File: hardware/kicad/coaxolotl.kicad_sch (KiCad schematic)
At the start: 0 parts

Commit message: Schematic v0.2: Olimex-style redraw with block diagram
- power/ground only as power symbols (project rails VCOAX, VMAIN, VHOLD, VLED, LNA_VCC)
- wires inside blocks, hierarchical labels + sheet pins between sheets (no global labels)
- Value carries critical parameters, blue design-intent notes, bold italic block titles
- sheet 1: block diagram + wired hierarchy; RF/Panel placeholders with reset-safe pulls
- pull-downs moved to the receiving parts (TPS2553 EN, RF switches), RC filters to the ADC pins
- check.py compares net partitions (catches shorts and splits), generator flags 4-way junctions
- net classes in .kicad_pro (POWER 0.4 mm <= 1.25 x SC-70 pad)

Co-Authored-By: Claude Opus 5.5 <noreply@anthropic.com>
Claude-Session: https://claude.ai/code/session_01YRUiF8Vp4242sya9Xyg3TV
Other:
- added sheet Panel (panel.kicad_sch)
- added sheet RF (rf.kicad_sch)
- sheet MCU ports: added FAULT_N, FMN, ILNA, LED_OE_N, LED_RCK, LED_SCK, LED_SER, LNA_EN, LNA_PATH, SCAP_ADC, SENSE, SW_V1, SW_V2, SW_V3; removed none
- sheet Power ports: added FAULT_N, ILNA, LNA_EN, SCAP_ADC, SENSE; removed none
- note added: "+3V3"
- note added: "20 kHz-2 GHz"
- note added: "330uF || 0.1F"
- note added: "3V3 LDO"
- note added: "6x 74HC595, 48 lamps"
- note added: "8 FILTERS"
- note added: "88-108 MHz, opt."
- note added: "<- DC 4.5 V + OOK"
- note added: "ANTENNA"
- note added: "BIAS-T"
- note added: "COAX"
- note added: "Coaxolotl - block diagram"
- note added: "F0 THRU..F7"
- note added: "FB + 47uF"
- note added: "FM NOTCH"
- note added: "FMN"
- note added: "FRONT PANEL"
- note added: "GDT, limiter"
- note added: "HOLD-UP"
- note added: "HPF 25M, LPF 2.2G"
- note added: "IDEAL DIODE"
- note added: "LAMP RAIL"
- note added: "LED bus"
- note added: "LM66100"
- note added: "LNA"
- note added: "LNA SUPPLY"
- note added: "LNA_PATH"
- note added: "LNA_VCC"
- note added: "MCP1700"
- note added: "MCU (sheet 3)"
- note added: "MCU EFM8BB21"
- note added: "PE42520"
- note added: "PE42582"
- note added: "PRESELECTOR"
- note added: "PROTECTION"
- note added: "Power and ground cross sheets only as power symbols (VCOAX, VMAIN, VHOLD, VLED, LNA_VCC, +3V3, GND)."
- note added: "RF -> RTL-SDR V3"
- note added: "RF signal path (sheet 4)"
- note added: "SENSE, 680R, PWR"
- note added: "SP8T"
- note added: "SPDT"
- note added: "SW_V1..3"
- note added: "Sheets"
- note added: "Signals cross sheets as hierarchical labels through the sheet pins above. Firmware pin map: firmware/src/hal_efm8bb2.c"
- note added: "TPS2553+INA180"
- note added: "VCOAX"
- note added: "VCOAX TAP"
- note added: "VHOLD"
- note added: "VLED"
- note added: "VMAIN"
- note added: "bypass (F1-F4 force it: AUTO)"
- note added: "control (blue, dashed): LNA_PATH, SW_V1..3, FMN, LNA_EN"
- note added: "decodes OOK on SENSE, Snooze when idle"
- note added: "monitors SENSE, SCAP_ADC, ILNA, FAULT_N"
- note added: "panel (sheet 5)"
- note added: "power (sheet 2)"
- note added: "~100 mA"
- note removed: "2 Power - VCOAX tap, LM66100 ideal diode, TPS2553 + INA180 LNA supply, hold-up, 3V3 [this review]"
- note removed: "3 MCU - EFM8BB21F16G, C2, reset-safe pulls, test points [this review]"
- note removed: "4 RF - antenna protection, LNA/bypass SPDTs, preselector, FM notch, 2x PE42582, 8 filters, bias-T [next]"
- note removed: "5 Panel - 6x 74HC595, 48 lamps [next]"
- note removed: "COAXOLOTL"
- note removed: "Conventions: nets in CAPS with global labels cross sheets. Every pin is labelled (no long wires),"
- note removed: "Firmware pin map: firmware/src/hal_efm8bb2.c Design notes: docs/hardware.md"
- note removed: "Mast-head LNA + 8-way filter bank, powered and keyed over one coax by the RTL-SDR bias-T."
- note removed: "Sheets (review order):"
- note removed: "so the Python in hardware/kicad/tools/build.py is the source of truth."

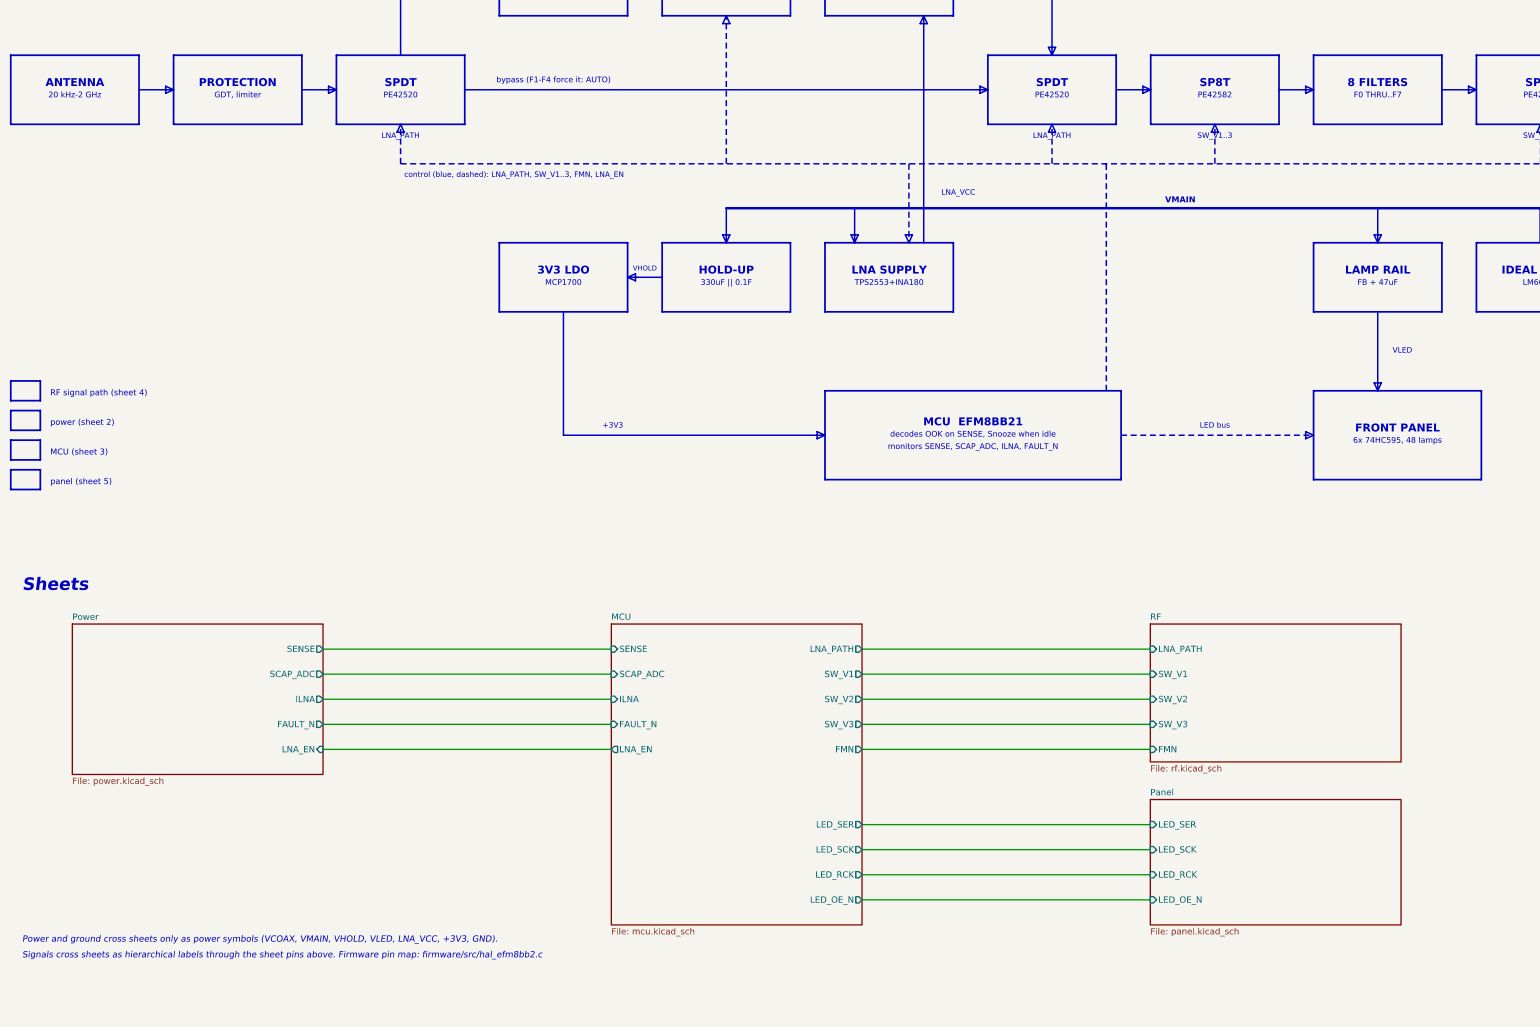
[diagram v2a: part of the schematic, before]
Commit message: Schematic: RF front end and filter bank sheets
- Sheet 4 RF front end: antenna protection (GDT, BAV99, 100k bleed),
  PE42522 LNA/bypass SPDT pair, 5th-order 25 MHz HPF + LTCC 2.2 GHz LPF,
  FM notch population option (DNP), LNA with bias through RFOUT.
- Sheet 5 filter bank: 2x PE42582 SP8T, F0 THRU + F1-F7 placeholders,
  broadband bias-T, coax connector, SW_V pull-downs.
- PE42522 replaces PE42520 (pinout could not be verified).
- Generator: mirrored symbols, stacked pins; root hierarchy for 6 sheets.
- gen_bandplan.py maps RF port index to the PE42582 V3V2V1 code.
- tools/bom.py: grouped BOM generated from the schematic.

Co-Authored-By: Claude Opus 5.5 <noreply@anthropic.com>
Claude-Session: https://claude.ai/code/session_01YRUiF8Vp4242sya9Xyg3TV
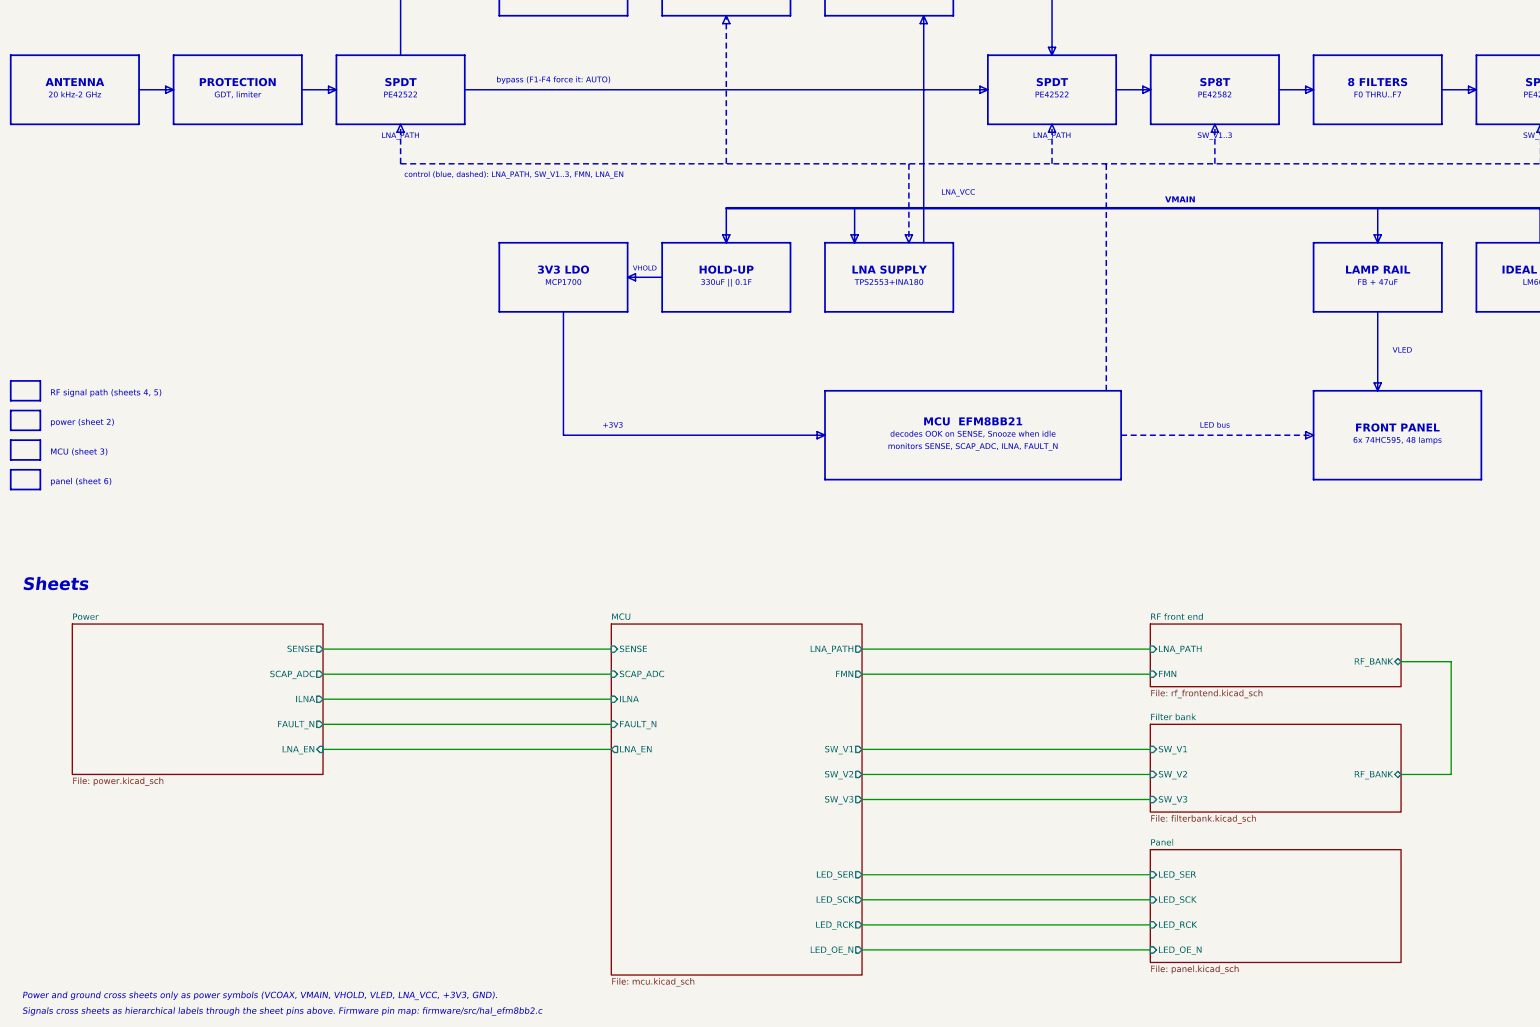
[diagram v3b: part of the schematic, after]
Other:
- removed sheet RF
- added sheet Filter bank (filterbank.kicad_sch)
- added sheet RF front end (rf_frontend.kicad_sch)
- note added: "PE42522"
- note added: "RF signal path (sheets 4, 5)"
- note added: "panel (sheet 6)"
- note removed: "PE42520"
- note removed: "RF signal path (sheet 4)"
- note removed: "panel (sheet 5)"
